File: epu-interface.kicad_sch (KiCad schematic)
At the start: 15 parts, among them J1 Conn_02x10_Odd_Even, J2 RJ11, J3 RJ11, J4 RJ11, J5 RJ11, U1 XRA1405, U2 74HC245, U3 74HC245

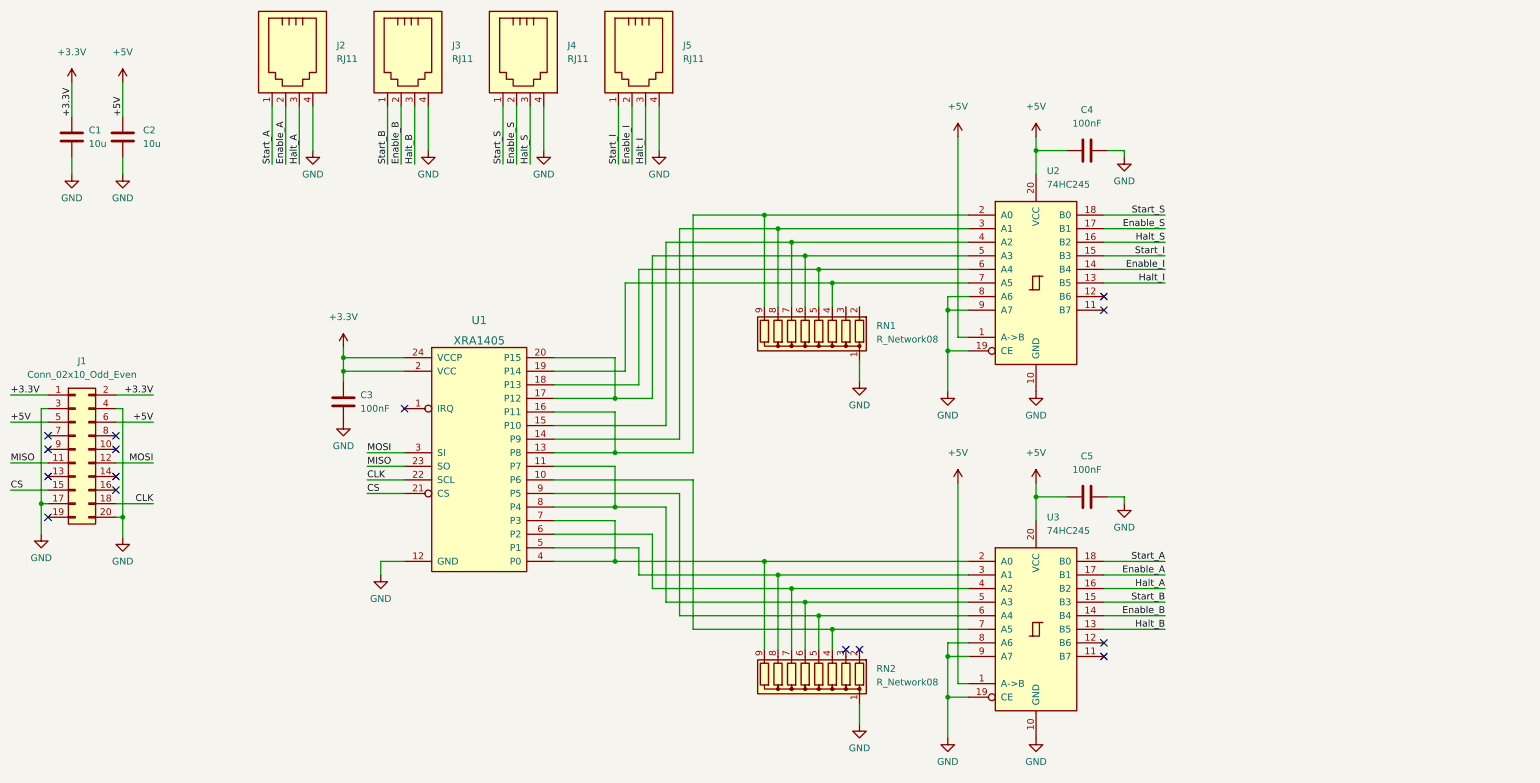
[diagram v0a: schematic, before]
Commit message: Changed 74HC245 to 74LS245
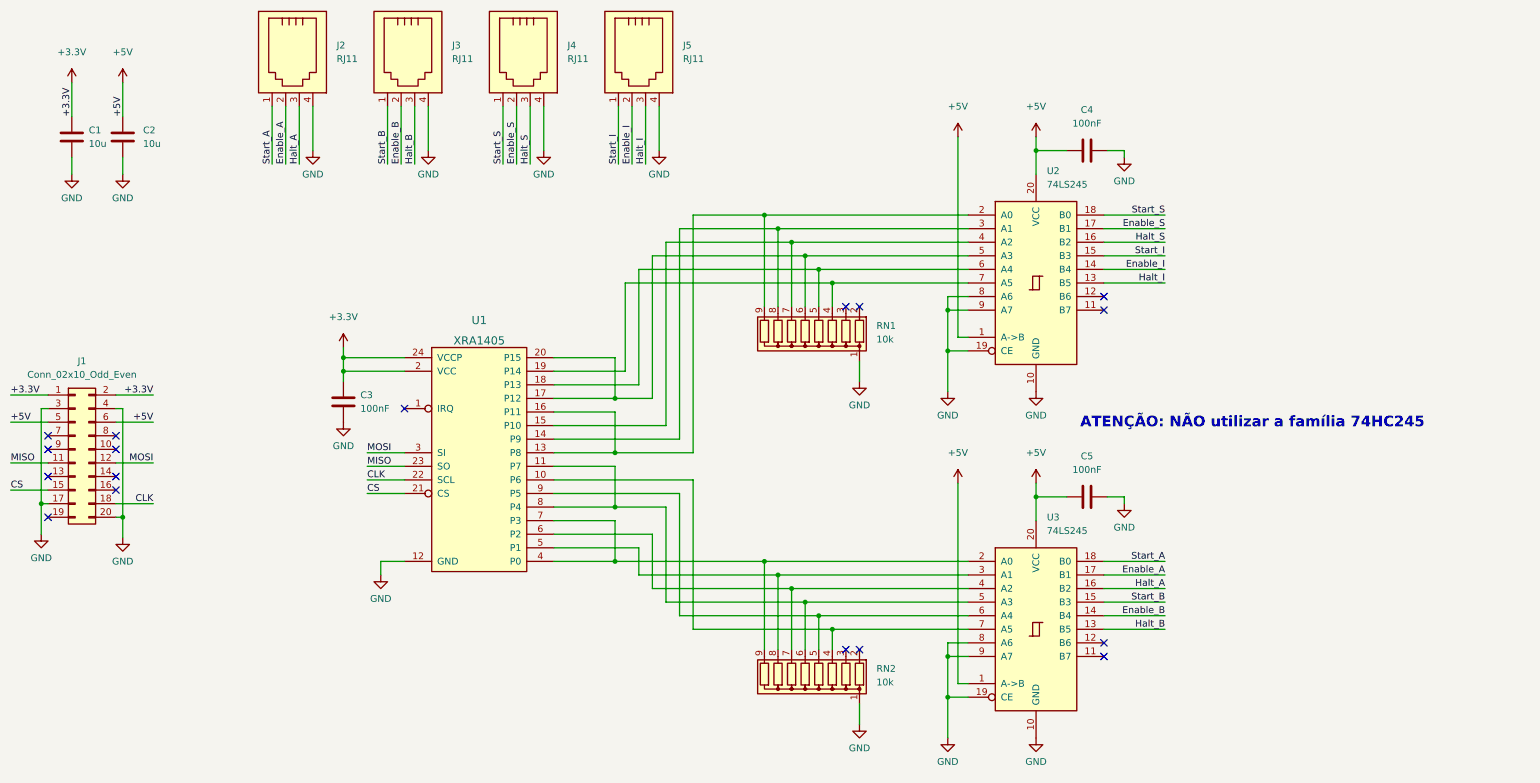
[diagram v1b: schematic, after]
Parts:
- RN1, RN2: value R_Network08 -> 10k
- U2, U3: value 74HC245 -> 74LS245
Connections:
- no-connect marks 15 -> 17
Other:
- note added: "ATENÇÃO: NÃO utilizar a família 74HC245"
- title: (none) -> EPU Interface Board
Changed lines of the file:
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@@
 (kicad_sch (version 20211123) (generator eeschema)
   (paper "A4")
+  (title_block
+    (title "EPU Interface Board")
+    (date "2022-10-10")
+    (rev "v0.1")
+    (comment 1 "Interface board for EPU control")
+    (comment 2 "Robert Polli & Rogério Marcondeli")
+  )
   (junction (at 170.815 133.985) (diameter 0) (color 0 0 0 0)
   )
@@
   (no_connect (at 224.155 74.295))
   (no_connect (at 93.345 95.25))
+  (no_connect (at 175.895 76.2))
+  (no_connect (at 178.435 76.2))
   (no_connect (at 224.155 141.605))
   (no_connect (at 224.155 139.065))
@@
     (stroke (width 0) (type default) (color 0 0 0 0))
   )
+  (text "ATENÇÃO: NÃO utilizar a família 74HC245" (at 219.71 99.06 0)
+    (effects (font (size 2 2) (thickness 0.254) bold) (justify left bottom))
+  )
   (label "MISO" (at 86.36 106.045 0)
     (effects (font (size 1.27 1.27)) (justify left bottom))
@@
       (effects (font (size 1.27 1.27)) (justify right))
     )
-    (property "Value" "R_Network08" (id 1) (at 181.61 82.2959 0)
+    (property "Value" "10k" (id 1) (at 181.61 82.2959 0)
       (effects (font (size 1.27 1.27)) (justify right))
     )
@@
       (effects (font (size 1.27 1.27)) (justify right))
     )
-    (property "Value" "R_Network08" (id 1) (at 181.61 146.4309 0)
+    (property "Value" "10k" (id 1) (at 181.61 146.4309 0)
       (effects (font (size 1.27 1.27)) (justify right))
     )
@@
       (effects (font (size 1.27 1.27)) (justify left))
     )
-    (property "Value" "74HC245" (id 1) (at 213.4744 53.34 0)
+    (property "Value" "74LS245" (id 1) (at 213.4744 53.34 0)
       (effects (font (size 1.27 1.27)) (justify left))
     )
@@
       (effects (font (size 1.27 1.27)) (justify left))
     )
-    (property "Value" "74HC245" (id 1) (at 213.4744 118.11 0)
+    (property "Value" "74LS245" (id 1) (at 213.4744 118.11 0)
       (effects (font (size 1.27 1.27)) (justify left))
     )
@@
     )
     (path "/1b7cd7a1-42ff-4681-b39b-a442453f42ae"
-      (reference "RN1") (unit 1) (value "R_Network08") (footprint "Resistor_THT:R_Array_SIP9")
+      (reference "RN1") (unit 1) (value "10k") (footprint "Resistor_THT:R_Array_SIP9")
     )
     (path "/2d72eab1-f6f2-4667-8d5e-50adba652ed0"
-      (reference "RN2") (unit 1) (value "R_Network08") (footprint "Resistor_THT:R_Array_SIP9")
+      (reference "RN2") (unit 1) (value "10k") (footprint "Resistor_THT:R_Array_SIP9")
     )
     (path "/df5ed5fe-38f3-48df-9cfa-e02815ddf0c8"
@@
     )
     (path "/40980ce8-4dc5-4aa9-93af-2a5bfc33f19c"
-      (reference "U2") (unit 1) (value "74HC245") (footprint "")
+      (reference "U2") (unit 1) (value "74LS245") (footprint "")
     )
     (path "/b62ba5e3-7dc3-4a03-8f56-c41b6e8dec0b"
-      (reference "U3") (unit 1) (value "74HC245") (footprint "")
-    )
-  )
+      (reference "U3") (unit 1) (value "74LS245") (footprint "")
+    )
+  )

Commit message: Added pcb layout
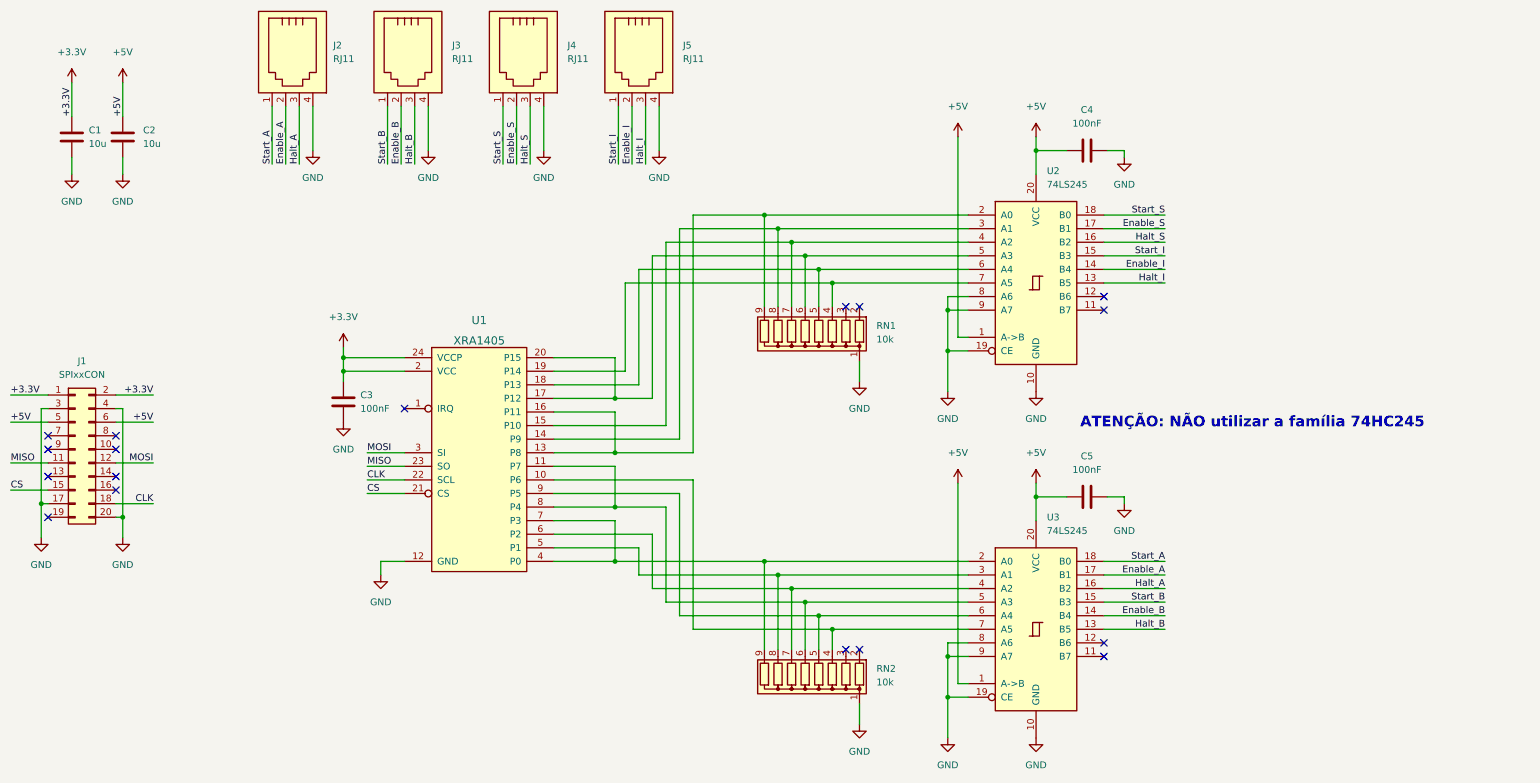
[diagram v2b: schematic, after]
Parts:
- C1, C2, C3, C4, C5: footprint (none) -> Capacitor_SMD:C_0805_2012Metric
- J1: value Conn_02x10_Odd_Even -> SPIxxCON; footprint (none) -> Connector_PinHeader_2.54mm:PinHeader_2x10_P2.54mm_Vertical
- J2, J3, J4, J5: footprint (none) -> Controle:RJ11_2
- U1: footprint (none) -> Package_SO:TSSOP-24_4.4x7.8mm_P0.65mm
- U2, U3: footprint (none) -> Package_SO:SOIC-20W_7.5x12.8mm_P1.27mm
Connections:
- net GND: now reaches C5.1
- net GND: now also C1.2, C2.2, C3.2, C4.1, J1.17 (Pin_17), J1.20 (Pin_20), J1.3 (Pin_3), J1.4 (Pin_4), J2.4, J3.4, J4.4, J5.4, RN1.1 (common), RN2.1 (common), U1.12 (GND), U2.10 (GND), U2.19 (CE), U2.8 (A6), U2.9 (A7), U3.10 (GND), U3.19 (CE), U3.8 (A6), U3.9 (A7)
